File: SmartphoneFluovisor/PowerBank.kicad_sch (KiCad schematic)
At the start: 35 parts, among them J1 USB_A, J2 Conn_01x02_Pin, J3 Conn_01x02, J4 Conn_01x02_Pin, J5 Conn_01x02_Pin, J6 Conn_01x02, SW1 SW_Push, U2 SC33063AD, X1 USB_C_24pins

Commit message: v0.3 connectors are on the same side
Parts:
- X1: footprint Shield1:FPC_12 -> Smartphone_Fluovisor:FPC_12
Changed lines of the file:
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@@
       (effects (font (size 1.27 1.27)))
     )
-    (property "Footprint" "Shield1:FPC_12" (at 38.1 77.47 0)
+    (property "Footprint" "Smartphone_Fluovisor:FPC_12" (at 38.1 77.47 0)
       (effects (font (size 1.27 1.27)) hide)
     )

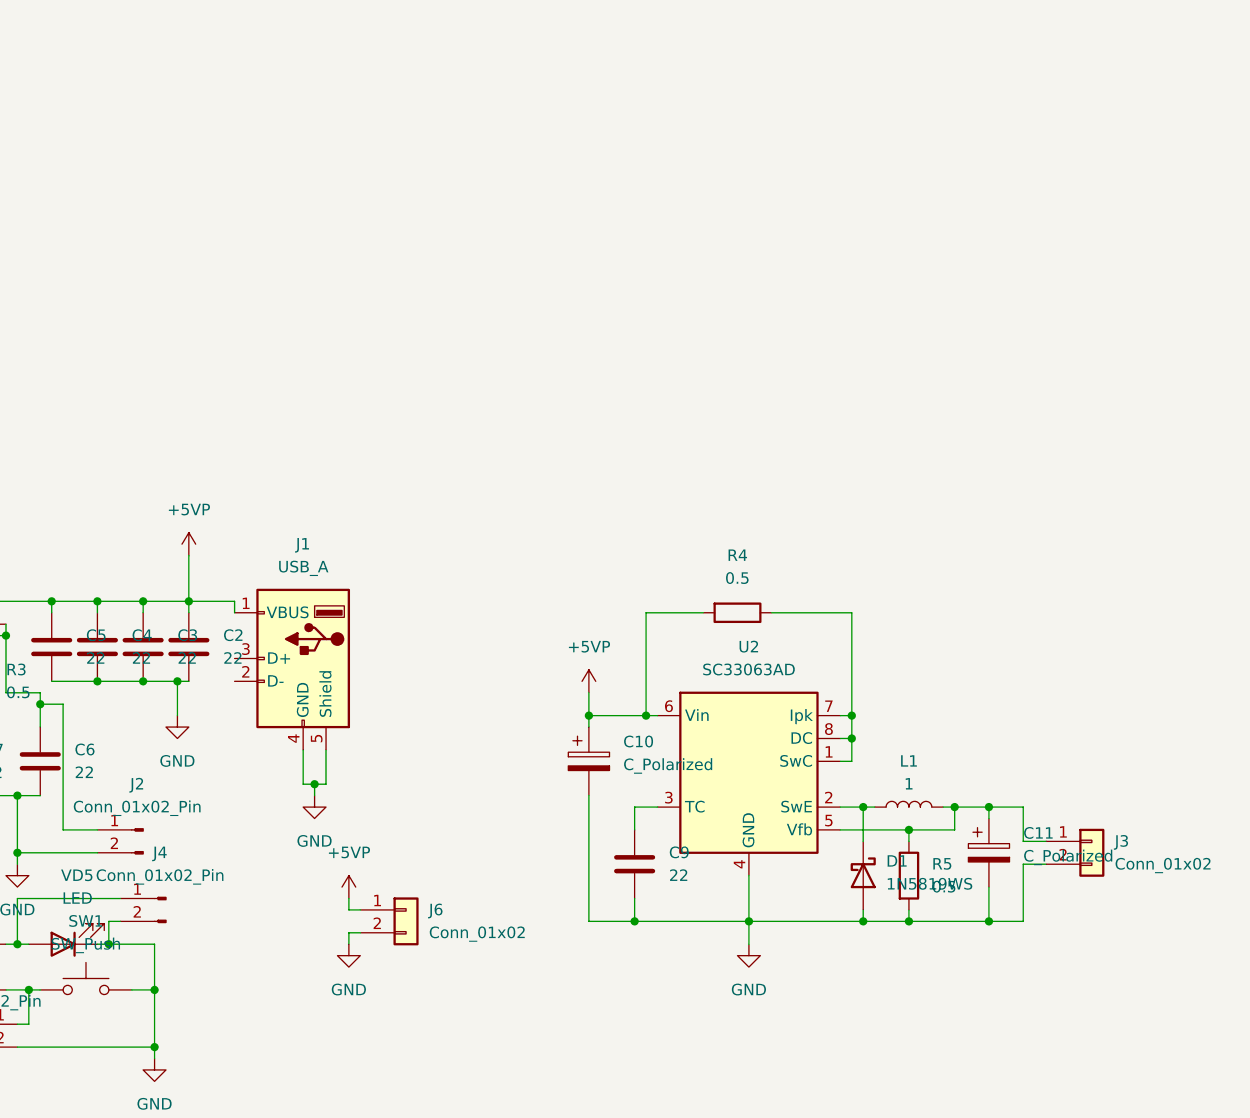
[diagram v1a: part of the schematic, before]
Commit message: v0.5 proto of boost driver was added
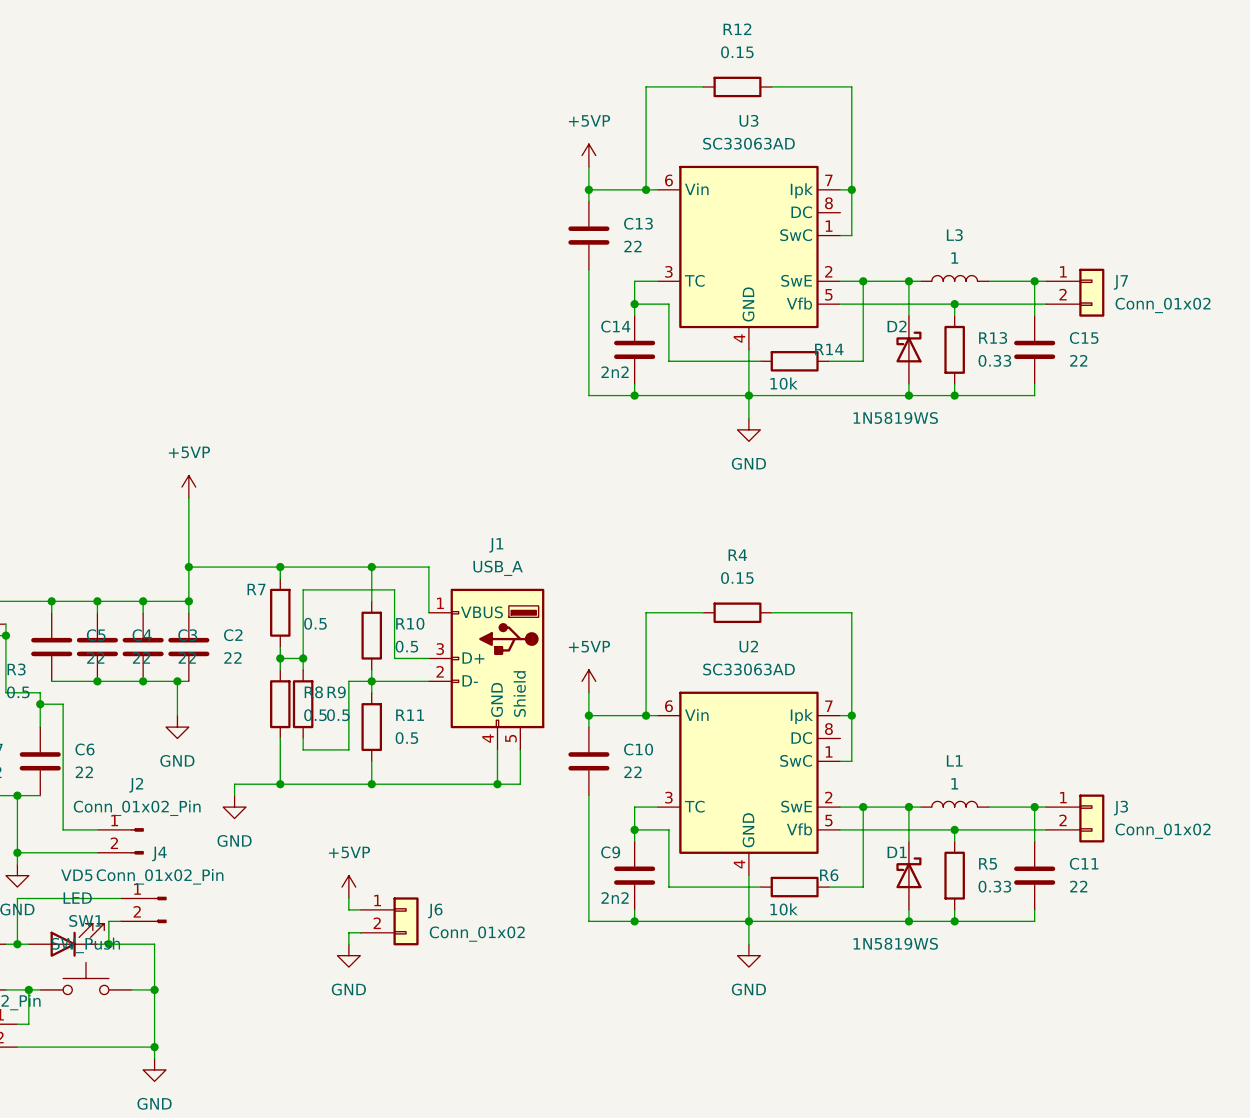
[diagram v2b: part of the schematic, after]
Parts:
- removed C10, C11: C_Polarized, Capacitor_SMD:CP_Elec_6.3x3, symbol Device:C_Polarized
- added C10, C11, C13, C15: 22, Capacitor_SMD:C_1206_3216Metric_Pad1.33x1.80mm_HandSolder, symbol Device:C
- added C14: 2n2, Capacitor_SMD:C_0603_1608Metric_Pad1.08x0.95mm_HandSolder, symbol Device:C
- added D2: 1N5819WS, Diode_SMD:D_SOD-323_HandSoldering, symbol Diode:1N5819WS
- added J7: Conn_01x02, Connector_PinHeader_2.54mm:PinHeader_1x02_P2.54mm_Vertical, symbol Connector_Generic:Conn_01x02
- added L3: 1, Inductor_SMD:L_12x12mm_H8mm, symbol Device:L
- added R10, R11, R7, R8, R9: 0.5, Resistor_SMD:R_0603_1608Metric_Pad0.98x0.95mm_HandSolder, symbol Device:R
- added R12: 0.15, Resistor_SMD:R_0603_1608Metric_Pad0.98x0.95mm_HandSolder, symbol Device:R
- added R13: 0.33, Resistor_SMD:R_1206_3216Metric_Pad1.30x1.75mm_HandSolder, symbol Device:R
- added R14, R6: 10k, Resistor_SMD:R_0603_1608Metric_Pad0.98x0.95mm_HandSolder, symbol Device:R
- added U3: SC33063AD, Package_SO:SOIC-8_3.9x4.9mm_P1.27mm, symbol Regulator_Switching:SC33063AD
- C9: value 22 -> 2n2
- L1: footprint Inductor_SMD:L_Vishay_IHLP-2525 -> Inductor_SMD:L_12x12mm_H8mm
- R4: value 0.5 -> 0.15
- R5: value 0.5 -> 0.33; footprint Resistor_SMD:R_0603_1608Metric_Pad0.98x0.95mm_HandSolder -> Resistor_SMD:R_1206_3216Metric_Pad1.30x1.75mm_HandSolder
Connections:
- net +5VP: now also C10.1, C13.1, R10.2, R12.2, R7.2, U3.6 (Vin)
- net GND: now also C10.2, C11.2, C13.2, C14.2, C15.2, D2.2 (A), R11.1, R13.2, R8.1, U3.4 (GND); no longer J3.2 (Pin_2)
- net at R4.1, U2.1 (SwC), U2.7 (Ipk): no longer U2.8 (DC)
- net at D1.1 (K), L1.1, U2.2 (SwE): now also R6.1
- net at C9.1, U2.3 (TC): now also R6.2
- net at J3.1 (Pin_1), L1.2: now also C11.1; no longer R5.1, U2.5 (Vfb)
- net at J1.2 (D-): now also R10.1, R11.2, R9.1
- net at J1.3 (D+): now also R7.1, R8.2, R9.2
- new net: R12.1, U3.1 (SwC), U3.7 (Ipk)
- new net: D2.1 (K), L3.1, R14.1, U3.2 (SwE)
- new net: J3.2 (Pin_2), R5.1, U2.5 (Vfb)
- new net: C14.1, R14.2, U3.3 (TC)
- new net: J7.2 (Pin_2), R13.1, U3.5 (Vfb)
- new net: C15.1, J7.1 (Pin_1), L3.2
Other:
- moved on the sheet: C9, D1, J1, J3, L1, R5

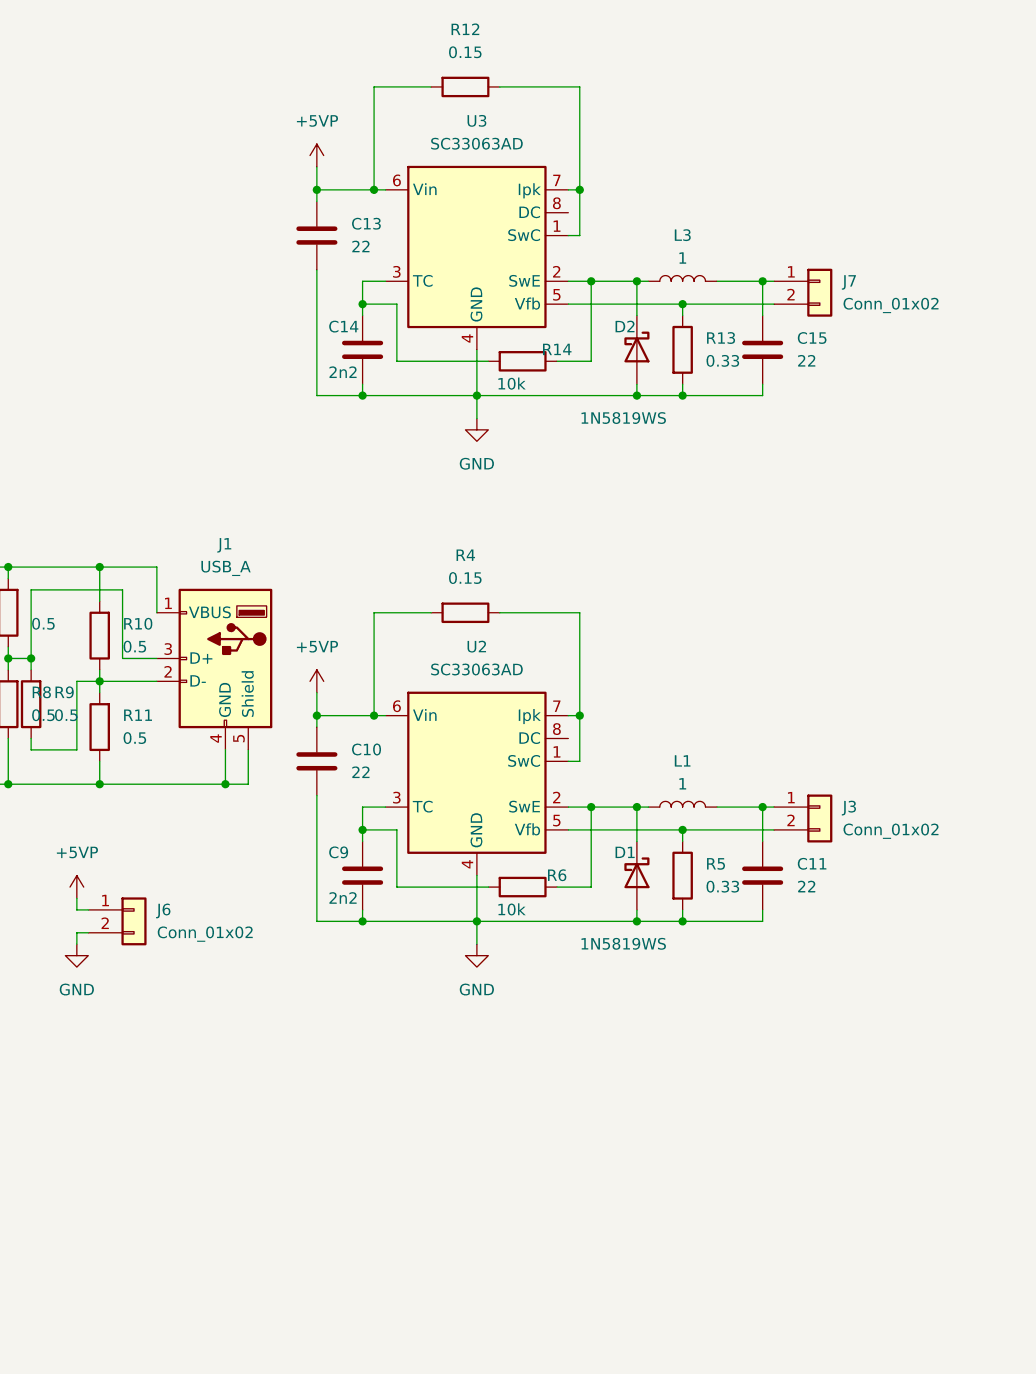
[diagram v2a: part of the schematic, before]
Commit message: v0.6 Circuit was completed, boost driver components were added onto PCB
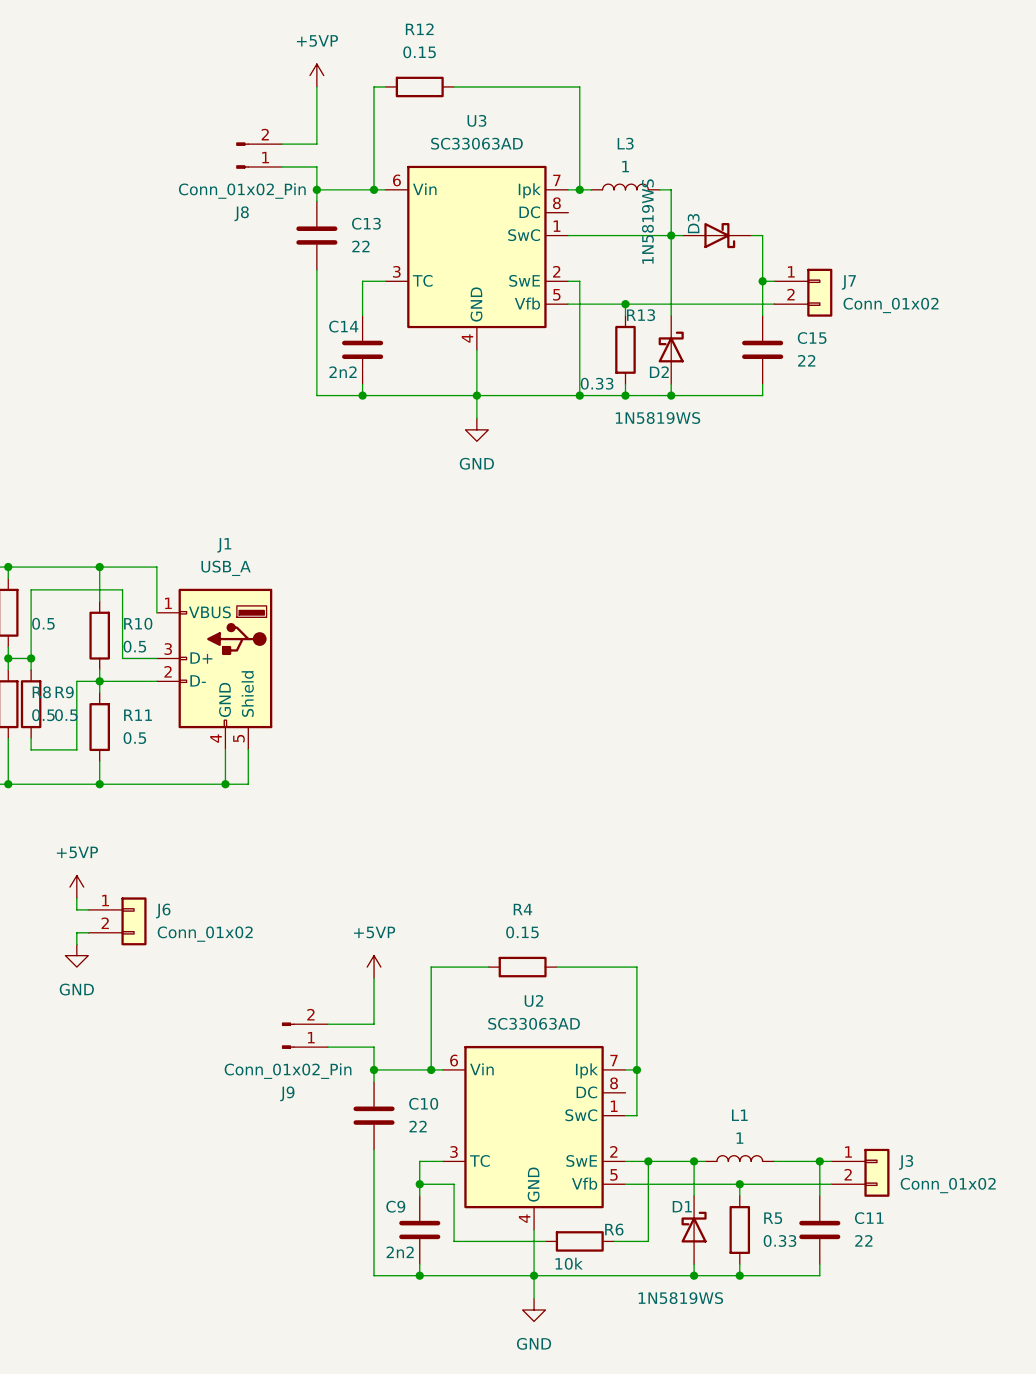
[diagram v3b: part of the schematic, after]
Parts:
- removed R14: 10k, Resistor_SMD:R_0603_1608Metric_Pad0.98x0.95mm_HandSolder, symbol Device:R
- added D3: 1N5819WS, Diode_SMD:D_SOD-323_HandSoldering, symbol Diode:1N5819WS
- added J8, J9: Conn_01x02_Pin, Connector_PinHeader_2.54mm:PinHeader_1x02_P2.54mm_Vertical, symbol Connector:Conn_01x02_Pin
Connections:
- net +5VP: now also J8.2 (Pin_2), J9.2 (Pin_2); no longer C10.1, C13.1, R12.2, R4.2, U2.6 (Vin), U3.6 (Vin)
- net GND: now also U3.2 (SwE)
- net at R12.1, U3.7 (Ipk): now also L3.1; no longer U3.1 (SwC)
- net at C15.1, J7.1 (Pin_1): now also D3.1 (K); no longer L3.2
- new net: C13.1, J8.1 (Pin_1), R12.2, U3.6 (Vin)
- new net: D2.1 (K), D3.2 (A), L3.2, U3.1 (SwC)
- new net: C10.1, J9.1 (Pin_1), R4.2, U2.6 (Vin)
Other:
- moved on the sheet: C10, C11, C9, D1, D2, J3, L1, L3, R12, R13, R4, R5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
